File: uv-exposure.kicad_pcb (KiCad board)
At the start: 2 copper layers, 180 x 120 mm, 147 parts, among them P1 CONN_1, P2 CONN_1, P3 CONN_1

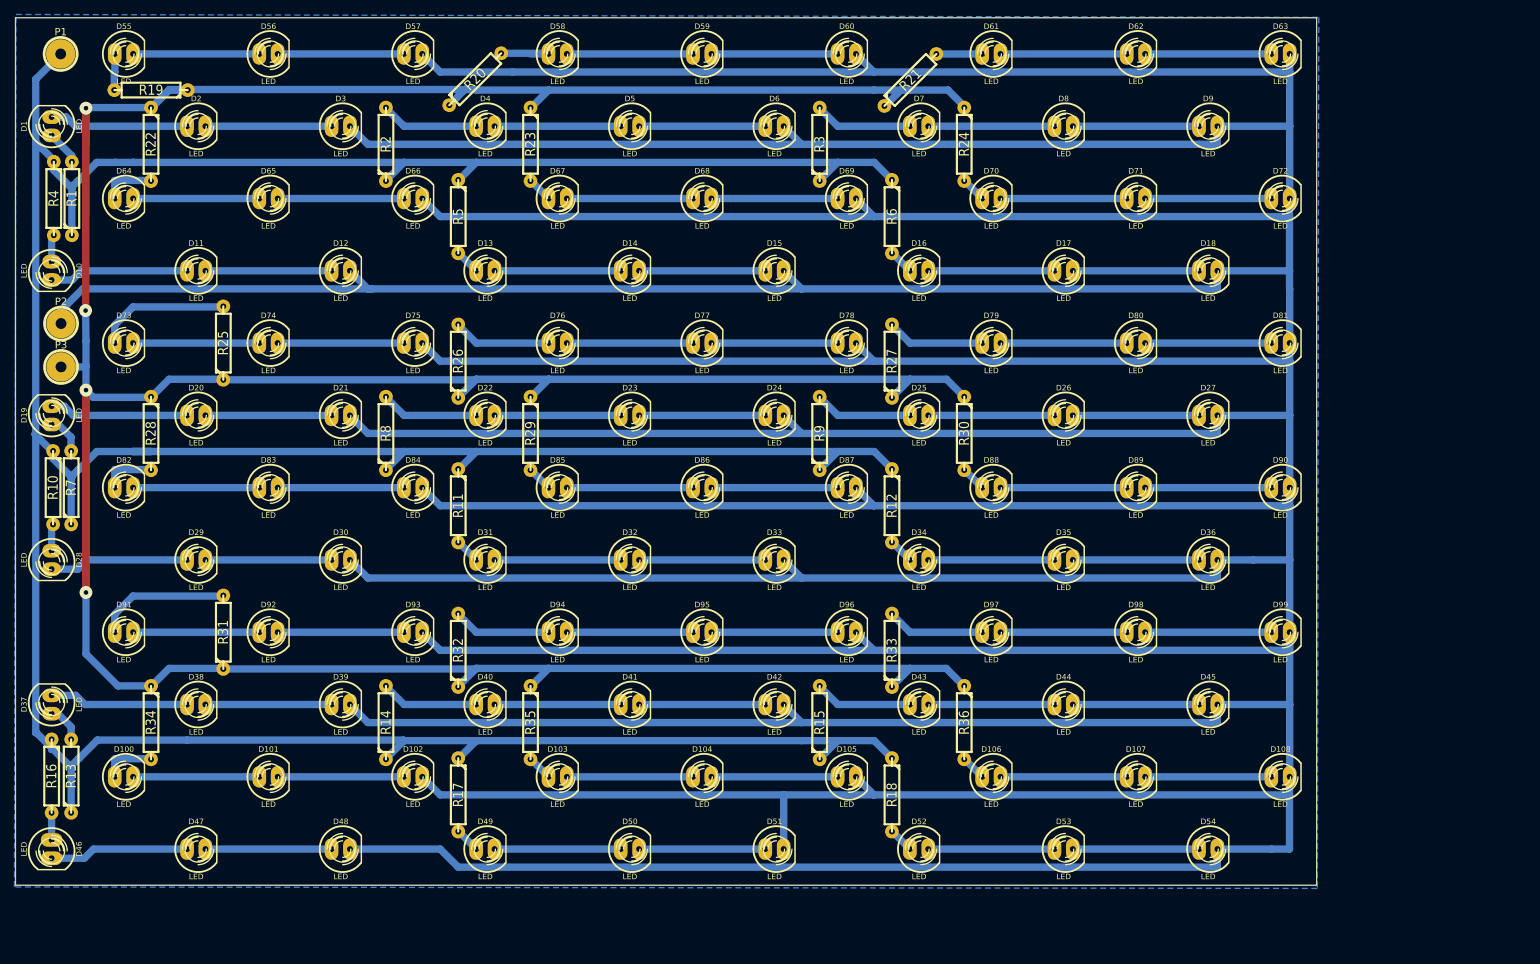
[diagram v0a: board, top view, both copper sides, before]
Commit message: All the leds now belong to the same subnet.
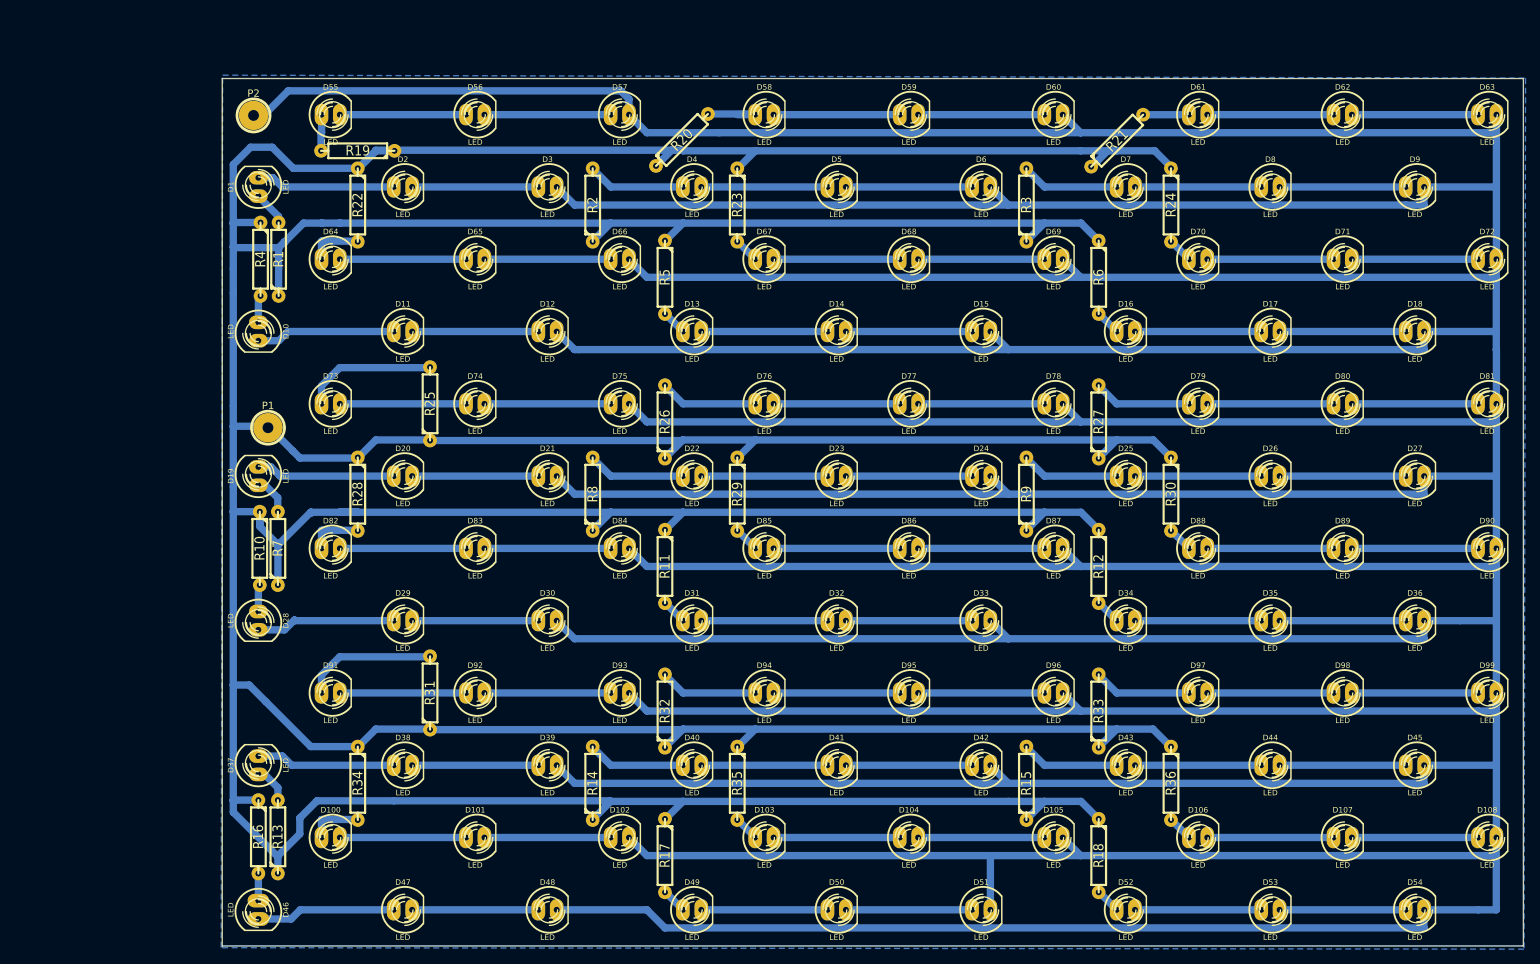
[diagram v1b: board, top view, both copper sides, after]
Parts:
- removed P3: CONN_1, 1pin
- moved P1 59.1 mm to (49.4, 72.0)
- moved P2 39.2 mm to (47.4, 28.8)
- moved D105 29.8 mm to (158.1, 128.7)
- moved D106 29.8 mm to (178.1, 128.7)
- moved D107 29.8 mm to (198.1, 128.7)
- moved D108 29.8 mm to (218.1, 128.7)
- moved D16 29.8 mm to (168.1, 58.7)
- moved D17 29.8 mm to (188.1, 58.7)
- moved D18 29.8 mm to (208.1, 58.7)
- moved D25 29.8 mm to (168.1, 78.7)
- moved D26 29.8 mm to (188.1, 78.7)
- moved D27 29.8 mm to (208.1, 78.7)
- moved D34 29.8 mm to (168.1, 98.7)
- moved D35 29.8 mm to (188.1, 98.7)
- moved D36 29.8 mm to (208.1, 98.7)
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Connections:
- R19 pad 1: VDD -> VCC
- R20 pad 1: VDD -> VCC
- R21 pad 1: VDD -> VCC
- R22 pad 1: VDD -> VCC
- R23 pad 1: VDD -> VCC
- R24 pad 1: VDD -> VCC
- R25 pad 1: VDD -> VCC
- R26 pad 1: VDD -> VCC
- R27 pad 1: VDD -> VCC
- R28 pad 1: VDD -> VCC
- R29 pad 1: VDD -> VCC
- R30 pad 1: VDD -> VCC
- R31 pad 1: VDD -> VCC
- R32 pad 1: VDD -> VCC
- R33 pad 1: VDD -> VCC
- R34 pad 1: VDD -> VCC
- R35 pad 1: VDD -> VCC
- R36 pad 1: VDD -> VCC
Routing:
- net VDD: track 490.1 -> 0.00 mm, vias 4 -> 0
- net VCC: track 527.4 -> 972.1 mm
- net GND: track 1732.4 -> 1742.4 mm
